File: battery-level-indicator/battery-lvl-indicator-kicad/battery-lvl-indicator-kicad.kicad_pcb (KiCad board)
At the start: 2 copper layers, 23.2 x 23.2 mm, 10 parts, among them J1 BT+, U1 LM393D

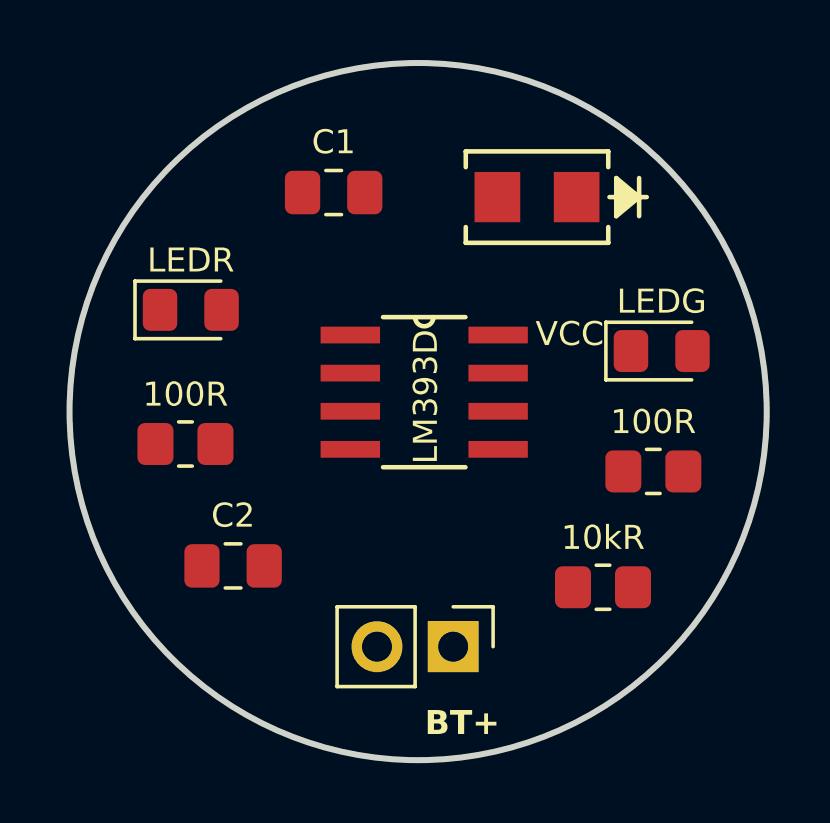
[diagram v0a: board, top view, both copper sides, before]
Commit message: Added connections to pcb.
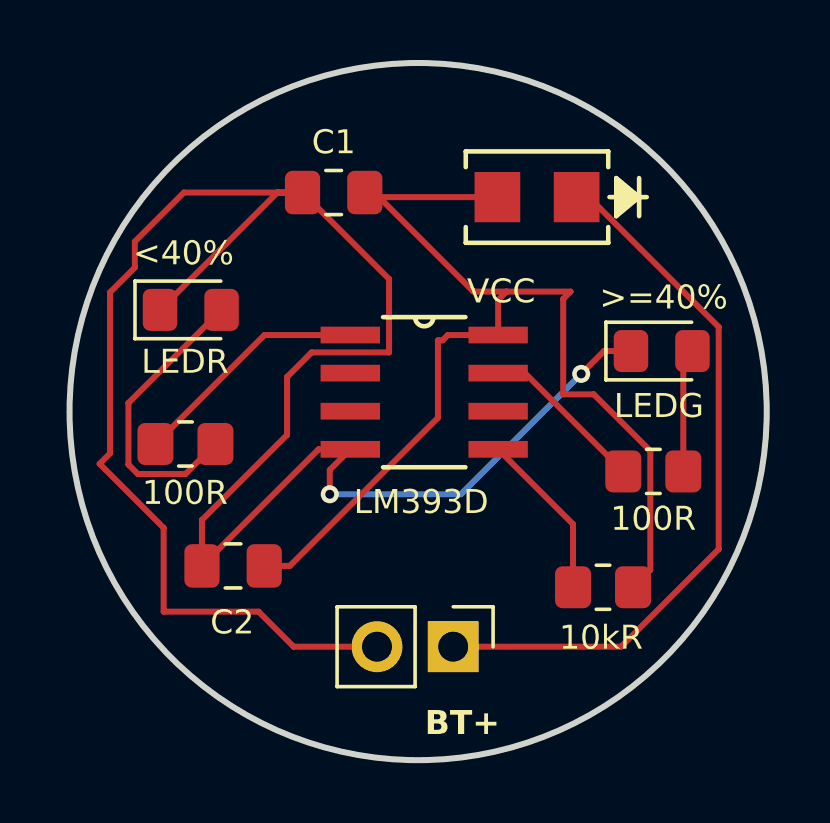
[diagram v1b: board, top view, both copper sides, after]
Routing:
- net Net-(D2-K): track 0.00 -> 73.8 mm, vias 0 -> 2
- net Net-(D1-A): track 0.00 -> 39.1 mm
- net Net-(D1-K): track 0.00 -> 24.1 mm
- net Net-(D2-A): track 0.00 -> 9.89 mm
- net Net-(U1-1OUT): track 0.00 -> 8.00 mm
- net Net-(U1-2IN+): track 0.00 -> 5.63 mm
- net Net-(U1-2OUT): track 0.00 -> 5.53 mm
- net Net-(D3-A): track 0.00 -> 4.14 mm
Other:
- board text added: "<40%"
- board text added: ">=40%"

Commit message: Added the gerber and drill files ready to order!
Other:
- board text added: "Battery level indicator"
- board text added: "Paco :3"
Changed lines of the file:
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@@
 			(outputformat 1)
 			(mirror no)
-			(drillshape 1)
+			(drillshape 0)
 			(scaleselection 1)
 			(outputdirectory "")
@@
 		(tags "resistor handsolder")
 		(property "Reference" "100R"
-			(at -0.016 1.6256 0)
+			(at -0.071772 1.8402 0)
 			(layer "F.SilkS")
 			(effects
@@
 		)
 		(fp_text user "${REFERENCE}"
-			(at 0 0 0)
+			(at -0.055772 0.2146 0)
 			(layer "F.Fab")
 			(effects
@@
 		(layer "Edge.Cuts")
 	)
+	(gr_text "Battery level \nindicator"
+		(at 155.0924 98.7552 0)
+		(layer "B.Cu")
+		(effects
+			(font
+				(size 1.5 1.5)
+				(thickness 0.3)
+				(bold yes)
+			)
+			(justify left bottom mirror)
+		)
+	)
+	(gr_text "Paco :3"
+		(at 152.7048 106.5276 0)
+		(layer "B.Cu")
+		(effects
+			(font
+				(size 1.5 1.5)
+				(thickness 0.3)
+				(bold yes)
+			)
+			(justify left bottom mirror)
+		)
+	)
 	(gr_text ">=40%"
